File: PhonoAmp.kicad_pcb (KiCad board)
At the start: 2 copper layers, 143.5 x 76.2 mm, 33 parts, among them J1 Screw_Terminal_01x03, J2 Screw_Terminal_01x03, J3 Screw_Terminal_01x02, U1 NE5532, U2 TL072

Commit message: Component Layout reviewed
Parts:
- added H1: MountingHole, MountingHole:MountingHole_3mm, F.Cu at (91.4, 69.8)
- added H2: MountingHole, MountingHole:MountingHole_3mm, F.Cu at (161.3, 69.8)
- added H3: MountingHole, MountingHole:MountingHole_3mm, F.Cu at (91.4, 113.0)
- added H4: MountingHole, MountingHole:MountingHole_3mm, F.Cu at (161.3, 113.0)
- C1, C11, C12, C13, C14, C2, C5, C6, C7, C8: footprint Capacitor_THT:CP_Radial_D8.0mm_P2.50mm -> Capacitor_THT:CP_Radial_D8.0mm_P3.50mm
- C10, C3, C4, C9: footprint Capacitor_THT:C_Disc_D5.0mm_W2.5mm_P2.50mm -> Capacitor_THT:C_Rect_L7.2mm_W2.5mm_P5.00mm_FKS2_FKP2_MKS2_MKP2
- R1, R10, R11, R12, R13, R2, R3, R4, R5, R6, R8, R9: footprint Resistor_THT:R_Axial_DIN0411_L9.9mm_D3.6mm_P15.24mm_Horizontal -> Resistor_THT:R_Axial_DIN0207_L6.3mm_D2.5mm_P7.62mm_Horizontal
- moved R1 107.8 mm to (101.6, 80.0), turned to 90 degrees
- moved C3 75.4 mm to (138.4, 82.5), turned to 180 degrees
- moved C4 65.4 mm to (149.8, 82.5), turned to 180 degrees
- moved R14 64.8 mm to (133.3, 111.8), turned to 180 degrees
- moved R4 61.9 mm to (132.1, 78.7)
- moved R7 58.0 mm to (133.3, 71.1), turned to 180 degrees
- moved C5 54.1 mm to (114.3, 72.4), turned to 90 degrees
- moved C14 50.3 mm to (130.8, 92.7), turned to 90 degrees
- moved C1 48.7 mm to (96.2, 80.0)
- moved C6 45.1 mm to (147.3, 69.8), turned to -90 degrees
- moved R2 43.9 mm to (105.4, 72.4), turned to -90 degrees
- moved R5 41.0 mm to (151.1, 78.7), turned to 180 degrees
- moved R3 40.2 mm to (119.4, 82.5), turned to 180 degrees
- moved J1 39.1 mm to (92.7, 88.9), turned to 0 degrees
- moved C11 37.6 mm to (114.3, 110.8), turned to -90 degrees
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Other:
- board size 143.5 x 76.2 mm -> 80 x 53.3 mm
- board text added: "12V-"
- board text added: "GND"
- board text added: "Input"
- board text added: "Output"

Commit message: iBom Production files Transferfunctions
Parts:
- C1, C7: footprint Capacitor_THT:CP_Radial_D8.0mm_P3.50mm -> Capacitor_THT:C_Rect_L7.2mm_W5.5mm_P5.00mm_FKS2_FKP2_MKS2_MKP2
- C10, C4: value 1n5 -> 1n
- C11, C12, C2, C5, C6, C8: footprint Capacitor_THT:CP_Radial_D8.0mm_P3.50mm -> Capacitor_THT:CP_Radial_D5.0mm_P2.00mm
- C3, C9: value 6n8 -> 10n
- R11, R4: value 750k -> 1M
- moved R3 7.62 mm to (111.8, 82.5), turned to 0 degrees
- moved R6 7.62 mm to (119.4, 78.7), turned to 180 degrees
- moved J3 2.01 mm to (125.1, 71.8)
- moved C2 1.80 mm to (158.8, 82.5)
- moved H1 1.80 mm to (92.7, 71.1)
- moved H3 1.80 mm to (92.7, 111.8)
- moved H2 1.80 mm to (160.0, 71.1)
- moved H4 1.80 mm to (160.0, 111.8)
- moved C11 1.58 mm to (114.3, 109.2)
- moved C8 1.31 mm to (158.8, 101.6)
- moved C6 1.27 mm to (147.3, 71.1)
- moved C12 1.27 mm to (147.3, 111.8)
- moved C5 1.27 mm to (114.3, 73.7)
- moved R14 0.64 mm to (133.3, 111.1)
- moved R7 0.63 mm to (133.3, 71.8)
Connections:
- C1 pad 1: /op1in+ -> /op1in+L
- C10 pad 1: /op2out -> /op2outR
- C2 pad 2: /op2out -> /op2outL
- C3 pad 2: /op2in- -> /op2in-L
- C4 pad 1: /op2out -> /op2outL
- C7 pad 1: /op1in+ -> /op1in+R
- C8 pad 2: /op2out -> /op2outR
- C9 pad 2: /op2in- -> /op2in-R
- R1 pad 1: /op1in+ -> /op1in+L
- R10 pad 1: /op1in- -> /op1in-R
- R10 pad 2: /op2in+ -> /op2in+R
- R11 pad 1: /op2in- -> /op2in-R
- R12 pad 1: /op2out -> /op2outR
- R13 pad 2: /op1in- -> /op1in-R
- R14 pad 1: /op2in- -> /op2in-R
- R2 pad 2: /op1in+ -> /op1in+L
- R3 pad 1: /op1in- -> /op1in-L
- R3 pad 2: /op2in+ -> /op2in+L
- R4 pad 1: /op2in- -> /op2in-L
- R5 pad 1: /op2out -> /op2outL
- R6 pad 2: /op1in- -> /op1in-L
- R7 pad 1: /op2in- -> /op2in-L
- R8 pad 1: /op1in+ -> /op1in+R
- R9 pad 2: /op1in+ -> /op1in+R
- U1 pad 1: /op2in+ -> /op2in+L
- U1 pad 2: /op1in- -> /op1in-L
- U1 pad 3: /op1in+ -> /op1in+L
- U1 pad 5: /op1in+ -> /op1in+R
- U1 pad 6: /op1in- -> /op1in-R
- U1 pad 7: /op2in+ -> /op2in+R
- U2 pad 1: /op2out -> /op2outL
- U2 pad 2: /op2in- -> /op2in-L
- U2 pad 3: /op2in+ -> /op2in+L
- U2 pad 5: /op2in+ -> /op2in+R
- U2 pad 6: /op2in- -> /op2in-R
- U2 pad 7: /op2out -> /op2outR
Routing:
- net /12V: track 0.00 -> 109.7 mm
- net /op2in+L: track 0.00 -> 28.4 mm
- net /op2in+R: track 0.00 -> 26.6 mm
- net /op2in-L: track 0.00 -> 25.4 mm
- net /op1in+L: track 0.00 -> 21.7 mm
- net /op2outR: track 0.00 -> 21.4 mm
- net /op2in-R: track 0.00 -> 21.4 mm
- net /op1in+R: track 0.00 -> 19.5 mm
- net /op2outL: track 0.00 -> 19.1 mm
- net Net-(C12-Pad1): track 0.00 -> 12.8 mm
- net Net-(C6-Pad1): track 0.00 -> 12.8 mm
- net /input_R: track 0.00 -> 12.7 mm
- net /op1in-L: track 0.00 -> 12.2 mm
- net Net-(C3-Pad1): track 0.00 -> 11.8 mm
- net Net-(C10-Pad2): track 0.00 -> 11.8 mm
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- added copper zone on B.Cu, net GND
- added copper zone on F.Cu, net GND
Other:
- board size 80 x 53.3 mm -> 77.5 x 50.8 mm
- board text added: "12V"
- board text added: "Amp L"
- board text added: "Amp R"
- board text added: "G R L"
- board text added: "L R G"
- board text added: "SloBloLabs - Phono Preamp 0v01"
- board text removed: "12V-"

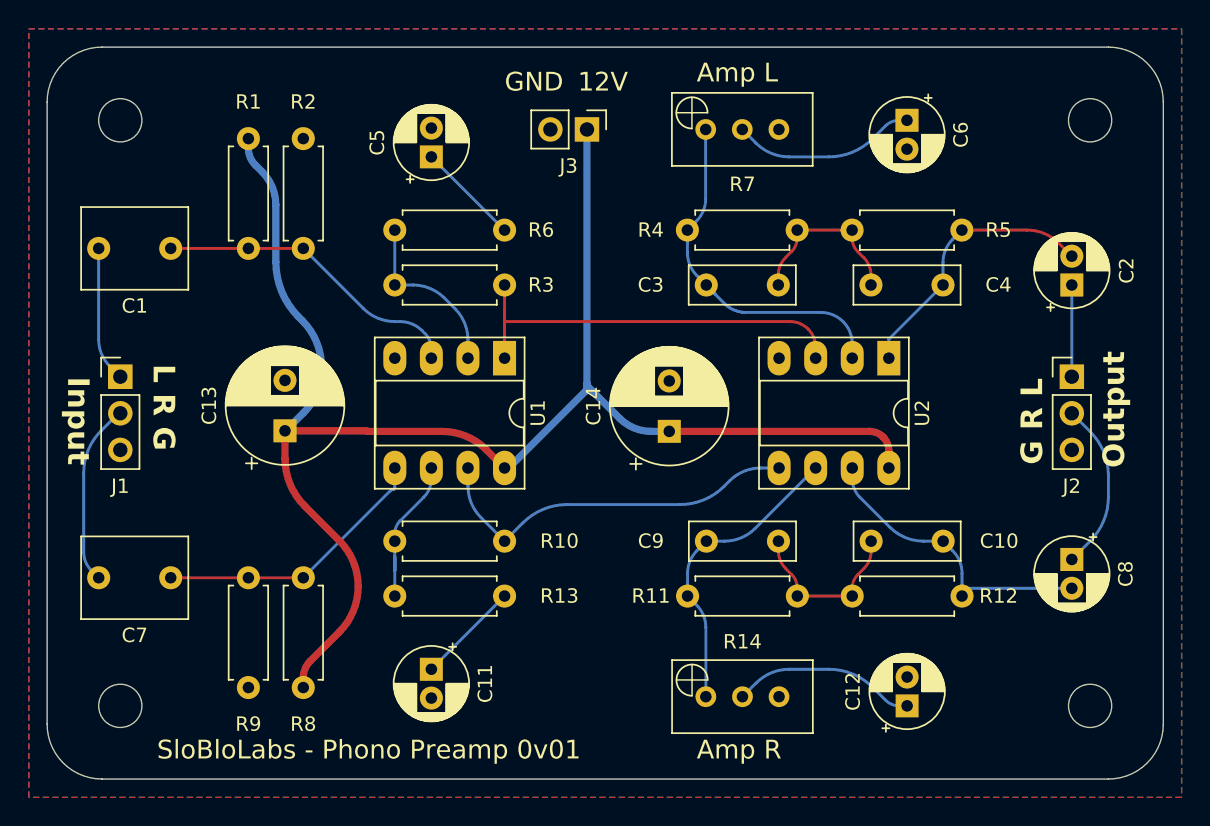
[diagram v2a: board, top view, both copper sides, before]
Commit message: Ordered Version 0v01 Rounded version in separate file Mounting holes aligned with Dual 626 chassis Optimized power supply tracks
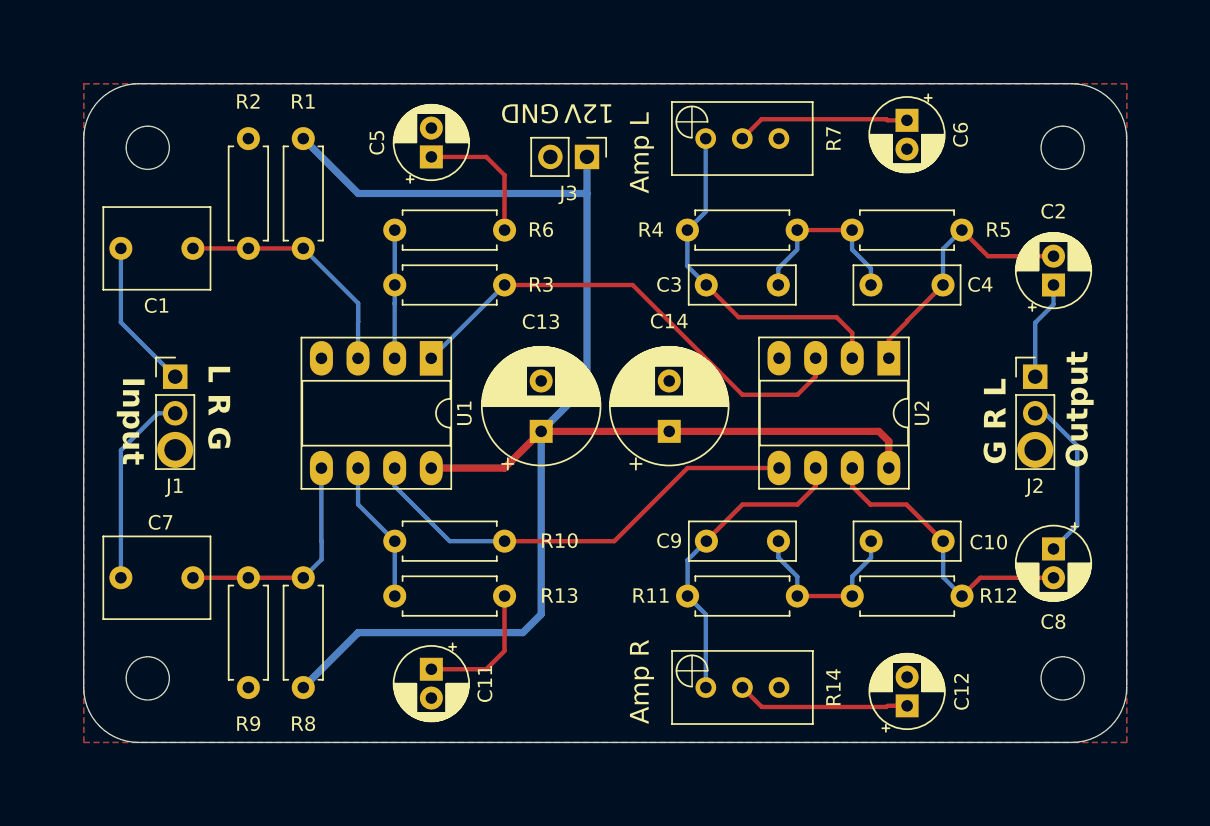
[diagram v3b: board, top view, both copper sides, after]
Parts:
- moved C13 17.8 mm to (121.9, 92.7)
- moved U1 5.09 mm to (114.3, 87.6)
- moved R1 3.81 mm to (105.4, 80.0)
- moved R2 3.81 mm to (101.6, 72.4)
- moved J1 3.81 mm to (96.5, 88.9)
- moved H1 2.69 mm to (94.6, 73.0)
- moved H2 2.69 mm to (158.1, 73.0)
- moved H3 2.69 mm to (94.6, 109.9)
- moved H4 2.69 mm to (158.1, 109.9)
- moved J2 2.54 mm to (156.2, 88.9)
- moved J3 1.91 mm to (125.1, 73.7)
- moved C1 1.54 mm to (97.8, 80.0)
- moved C7 1.54 mm to (97.8, 102.9)
- moved C8 1.46 mm to (157.5, 100.9)
- moved C2 1.27 mm to (157.5, 82.5)
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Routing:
- net /op2in+L: track 28.4 -> 33.8 mm
- net /op2in+R: track 26.6 -> 31.6 mm
- net /op1in+L: track 21.7 -> 16.9 mm
- net /op1in+R: track 19.5 -> 15.8 mm
- net /op1in-L: track 12.2 -> 8.90 mm
- net Net-(C11-Pad1): track 7.18 -> 9.42 mm
- net Net-(C5-Pad1): track 7.18 -> 9.42 mm
- net /12V: track 109.7 -> 107.9 mm
- net /input_L: track 9.40 -> 10.5 mm
- net /op2outR: track 21.4 -> 20.4 mm
- net /op2outL: track 19.1 -> 18.1 mm
- net /input_R: track 12.7 -> 13.7 mm
- net /op2in-L: track 25.4 -> 24.5 mm
- net Net-(C12-Pad1): track 12.8 -> 12.0 mm
- net Net-(C6-Pad1): track 12.8 -> 12.0 mm
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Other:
- board size 77.5 x 50.8 mm -> 72.4 x 45.7 mm

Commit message: Simulation and Optimization
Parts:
- C10, C4: value 1n -> 10n
- C12, C6: value 22u -> 10u
- C3, C9: value 10n -> 47n
- R11, R4: value 1M -> 220k
- R12, R5: value 51k -> 10k
